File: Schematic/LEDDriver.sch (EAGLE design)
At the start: 33 parts, among them IC1 TL494CN, IC2 LM317, IC3 TL494CN, Q1 IRFZ44N, Q2 IRFZ44N, Q3 BC557, Q4 BC557

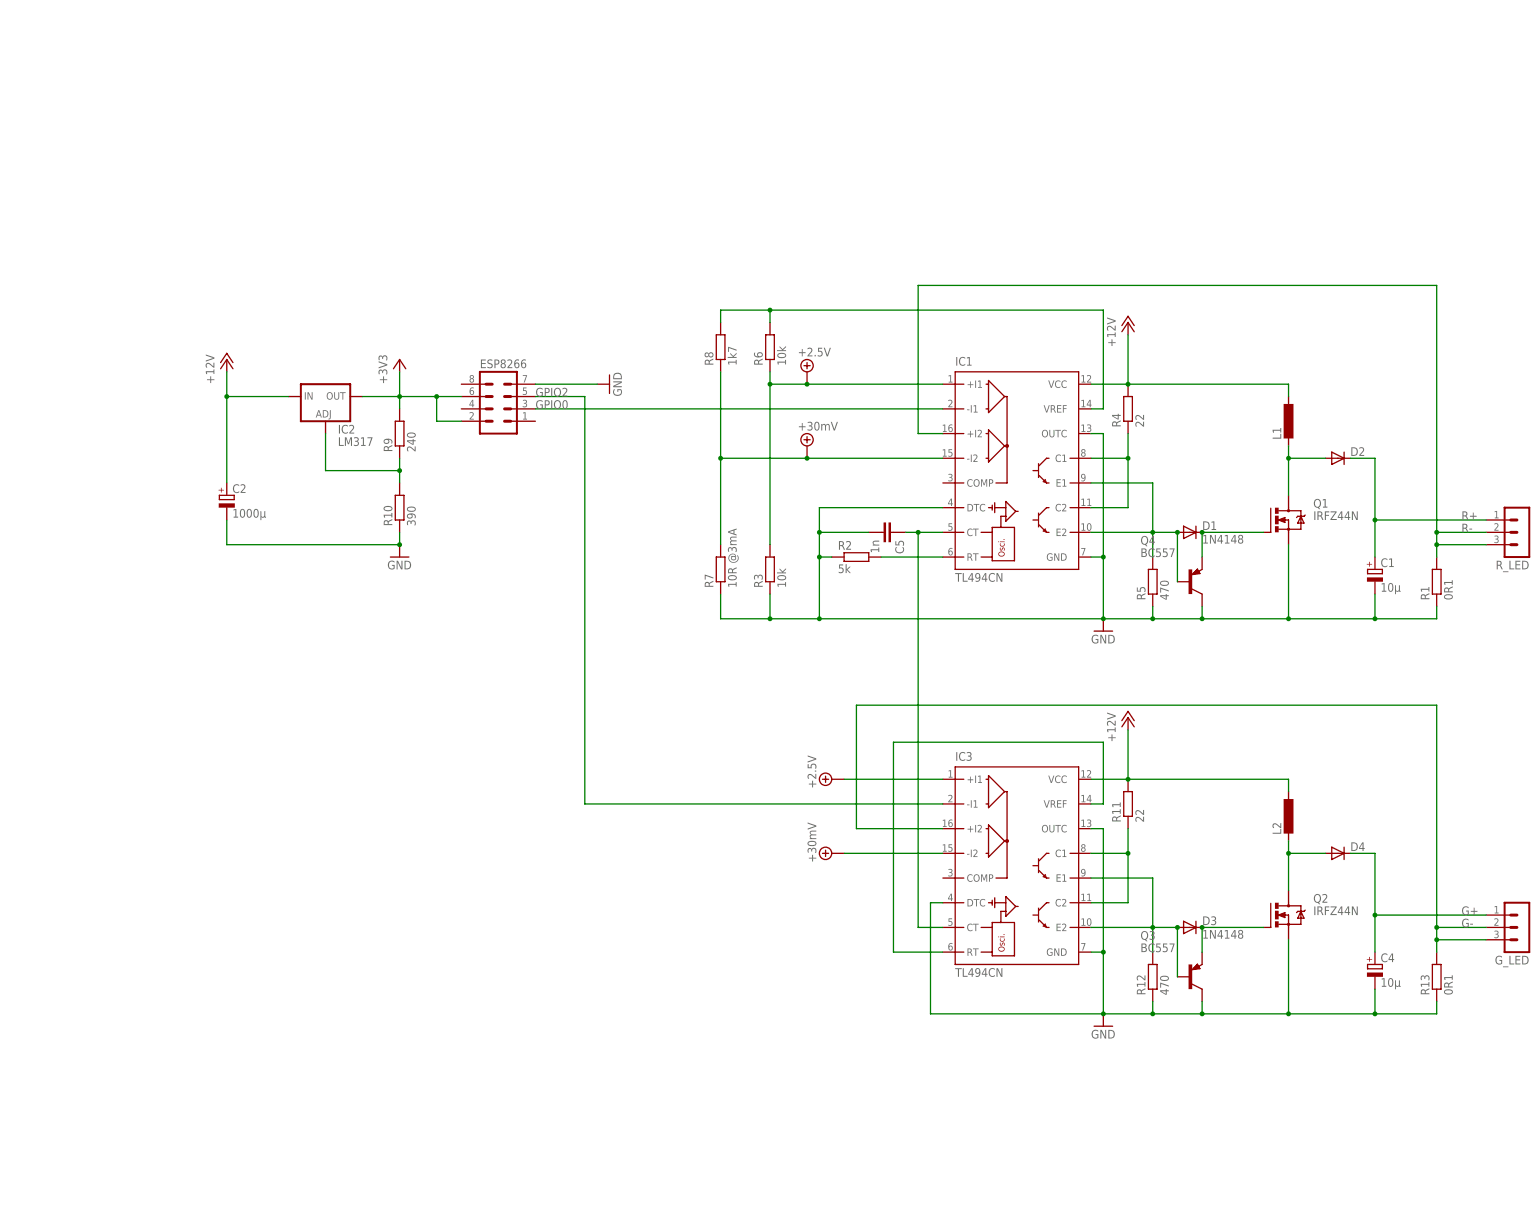
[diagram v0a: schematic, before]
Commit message: Use Xl6009 with op amp as  current source for leds
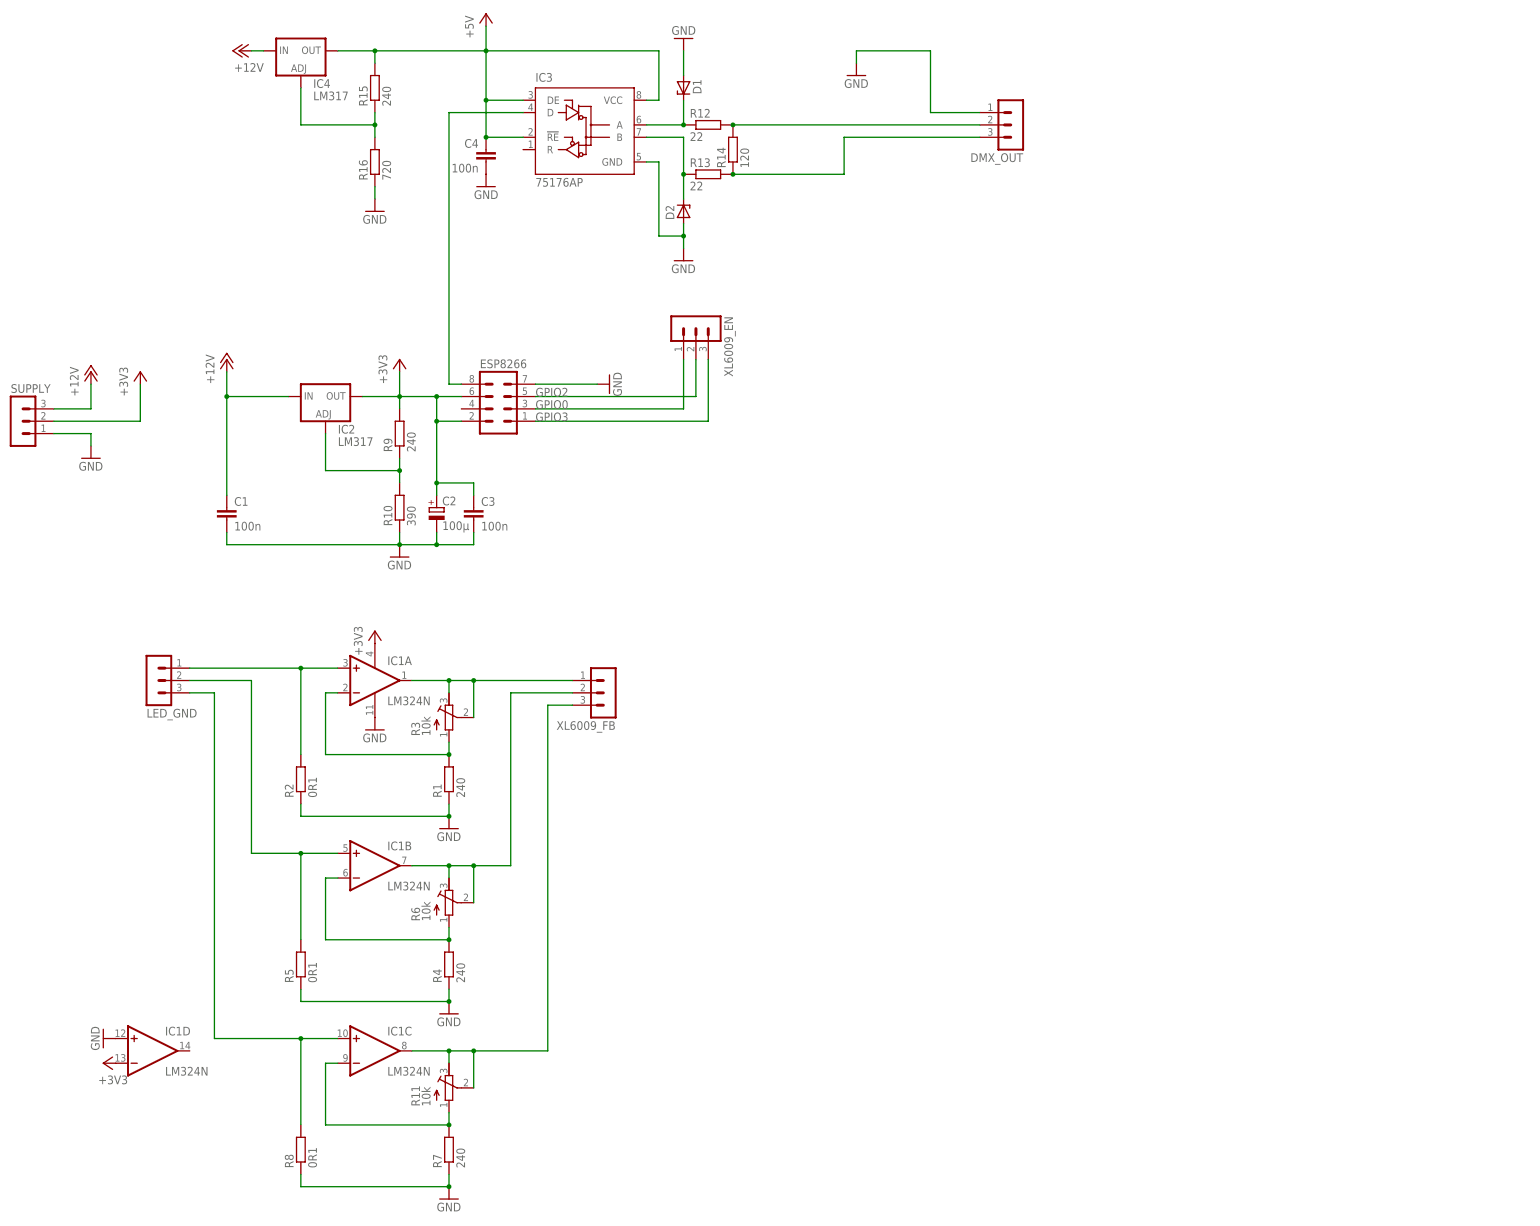
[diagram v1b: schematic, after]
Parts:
- removed C5: 1n, rcl:C-EU025-024X044
- removed D3: 1N4148, diode:DIODE-D-2.5
- removed D4: (no value), diode:DIODE-D-2.5
- removed G_LED, R_LED: (no value), con-lstb:MA03-1
- removed L1, L2: (no value), rcl:L-EU0204/5
- removed Q1, Q2: IRFZ44N, transistor-power:IRFZ48Z
- removed Q3, Q4: BC557, transistor-pnp:BC557
- added C3: 100n, rcl:C-EU075-032X103
- added DMX_OUT, LED_GND, SUPPLY, XL6009_EN, XL6009_FB: (no value), con-lstb:MA03-1
- added IC4: LM317, v-reg:LM317TS
- added R14: 120, rcl:R-EU_0204/2V
- added R15: 240, rcl:R-EU_0204/2V
- added R16: 720, rcl:R-EU_0207/10
- C1, C4: value 10µ -> 100n; device rcl:CPOL-EUE2.5-6 -> rcl:C-EU075-032X103
- C2: value 1000µ -> 100µ
- D1: value 1N4148 -> (none); device diode:DIODE-D-2.5 -> diode:ZENER-DIODEZD-2.5
- D2: device diode:DIODE-D-2.5 -> diode:ZENER-DIODEDO34-7
- IC1: value TL494CN -> LM324N; device linear:TL494CN -> linear:LM324N
- IC3: value TL494CN -> 75176AP; device linear:TL494CN -> 751xx:75176AP
- R1: value 0R1 -> 240; device rcl:R-EU_0204/7 -> rcl:R-EU_0204/2V
- R10: device rcl:R-EU_0207/10 -> rcl:R-EU_0207/12
- R11: value 22 -> 10k; device rcl:R-EU_0204/2V -> rcl:R-TRIMM64W
- R12: value 470 -> 22
- R13: value 0R1 -> 22; device rcl:R-EU_0204/7 -> rcl:R-EU_0204/2V
- R2: value 5k -> 0R1
- R3: device rcl:R-EU_0204/2V -> rcl:R-TRIMM64W
- R4: value 22 -> 240
- R5: value 470 -> 0R1
- R6: device rcl:R-EU_0204/7 -> rcl:R-TRIMM64W
- R7: value 10R @3mA -> 240
- R8: value 1k7 -> 0R1
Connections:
- removed net +30MV: IC1.-I2, IC3.-I2, R7.2, R8.1
- removed net +4.1V: IC1.+I1, IC3.+I1, R3.2, R6.1
- removed net G+: C4.+, D4.C, G_LED.1
- removed net G-: G_LED.2, G_LED.3, IC3.+I2, R13.2
- removed net N$17: IC3.C1, IC3.C2, R11.1
- removed net N$18: D3.A, IC3.E1, IC3.E2, Q3.B, R12.2
- removed net N$19: D4.A, L2.2, Q2.D
- removed net R+: C1.+, D2.C, R_LED.1
- removed net R-: IC1.+I2, R1.2, R_LED.2, R_LED.3
- new net +5V: C4.1, IC3.!RE, IC3.DE, IC3.VCC, IC4.OUT, R15.2
- new net DMX2: DMX_OUT.2, R12.2, R14.2
- new net GPIO3: ESP8266.1, XL6009_EN.3
- new net N$10: IC1C.+IN, LED_GND.3, R8.2
- new net N$14: D1.C, IC3.A, R12.1
- new net N$15: D2.C, IC3.B, R13.1
- new net N$4: IC1A.OUT, R3.E, R3.S, XL6009_FB.1
- new net N$9: IC1B.-IN, R4.2, R6.A
- net +12V: now also C1.1, IC4.IN, SUPPLY.3; no longer C2.+, IC1.VCC, IC3.VCC, L1.1, L2.1, R11.2, R4.2
- net +3V3: now also C2.+, C3.1, IC1D.-IN, IC1P.V+, SUPPLY.2
- net GND: now also C1.2, C3.2, C4.2, D1.A, D2.A, DMX_OUT.1, IC1D.+IN, IC1P.V-, R16.1, R4.1, R8.1, SUPPLY.1; no longer C1.-, C4.-, C5.2, IC1.DTC, IC1.GND, IC1.OUTC, IC3.DTC, IC3.OUTC, Q1.S, Q2.S, Q3.C, Q4.C, R12.1, R13.1, R3.1
- net GPIO0: now also XL6009_EN.1; no longer IC1.-I1
- net GPIO2: now also XL6009_EN.2; no longer IC3.-I1
- net N$1: now also ESP8266.8, IC3.D; no longer D2.A, L1.2, Q1.D
- net N$11: now also IC1C.OUT, R11.E, R11.S, XL6009_FB.3; no longer IC1.C1, IC1.C2, R4.1
- net N$12: now also IC1C.-IN, R11.A, R7.2; no longer D1.A, IC1.E1, IC1.E2, Q4.B, R5.2
- net N$16: now also DMX_OUT.3, R13.2, R14.1; no longer D3.C, Q2.G, Q3.E
- net N$2: now also IC1A.-IN, R1.2, R3.A; no longer C5.1, IC1.CT, IC3.CT
- net N$3: now also IC1A.+IN, LED_GND.1, R2.2; no longer IC3.RT, IC3.VREF
- net N$6: now also IC1B.+IN, LED_GND.2, R5.2; no longer IC1.RT, R2.2
- net N$7: now also IC1B.OUT, R6.E, R6.S, XL6009_FB.2; no longer IC1.VREF, R6.2, R8.2
- net N$8: now also IC4.ADJ, R15.1, R16.2; no longer D1.C, Q1.G, Q4.E
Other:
- moved on the sheet: C2, R1, R12, R13, R2, R4, R5, R7, R8

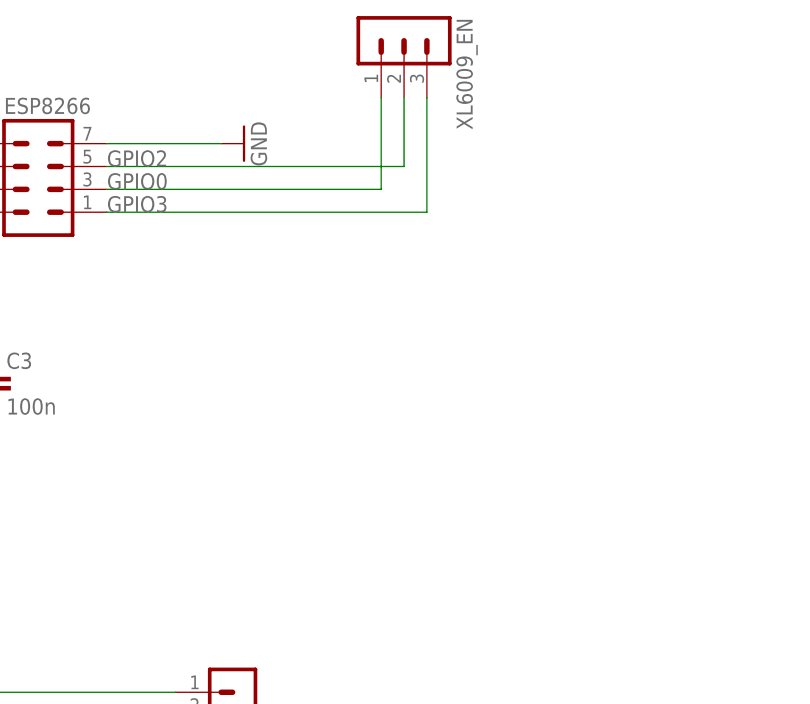
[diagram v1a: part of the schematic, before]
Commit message: Add pull downs to enable pins of LEDs to not flash up the LEDs on boot time
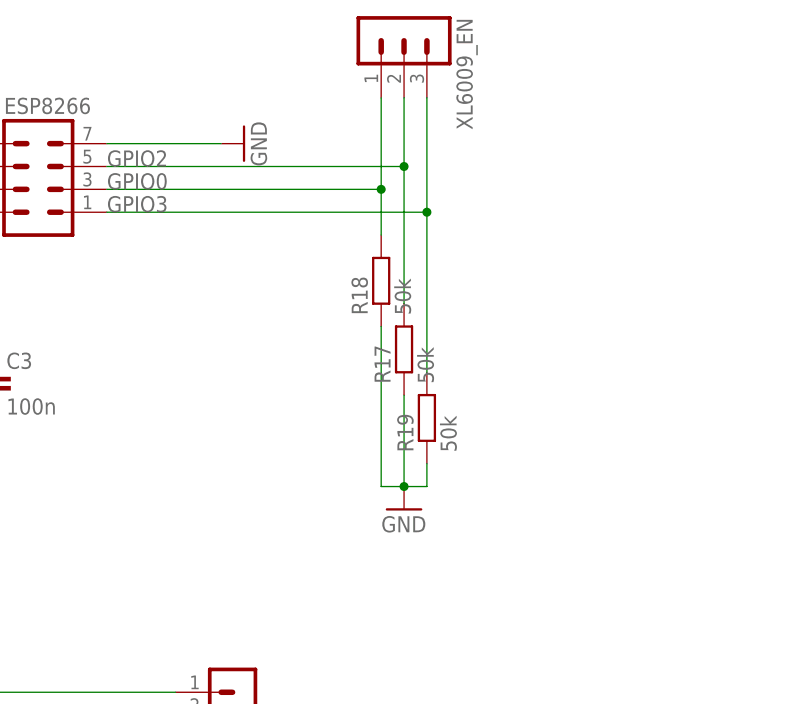
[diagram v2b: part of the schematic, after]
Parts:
- added R17, R18, R19: 50k, rcl:R-EU_0207/12
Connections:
- net GND: now also R17.1, R18.1, R19.1
- net GPIO0: now also R18.2
- net GPIO2: now also R17.2
- net GPIO3: now also R19.2
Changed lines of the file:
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@@
 <grid distance="0.1" unitdist="inch" unit="inch" style="lines" multiple="1" display="no" altdistance="0.01" altunitdist="inch" altunit="inch"/>
 <layers>
-<layer number="1" name="Top" color="4" fill="1" visible="yes" active="no"/>
-<layer number="16" name="Bottom" color="1" fill="1" visible="yes" active="no"/>
-<layer number="17" name="Pads" color="2" fill="1" visible="yes" active="no"/>
-<layer number="18" name="Vias" color="2" fill="1" visible="yes" active="no"/>
-<layer number="19" name="Unrouted" color="6" fill="1" visible="yes" active="no"/>
-<layer number="20" name="Dimension" color="15" fill="1" visible="yes" active="no"/>
-<layer number="21" name="tPlace" color="7" fill="1" visible="yes" active="no"/>
-<layer number="22" name="bPlace" color="7" fill="1" visible="yes" active="no"/>
-<layer number="23" name="tOrigins" color="15" fill="1" visible="yes" active="no"/>
-<layer number="24" name="bOrigins" color="15" fill="1" visible="yes" active="no"/>
-<layer number="25" name="tNames" color="7" fill="1" visible="yes" active="no"/>
-<layer number="26" name="bNames" color="7" fill="1" visible="yes" active="no"/>
-<layer number="27" name="tValues" color="7" fill="1" visible="yes" active="no"/>
-<layer number="28" name="bValues" color="7" fill="1" visible="yes" active="no"/>
+<layer number="1" name="Top" color="4" fill="1" visible="no" active="no"/>
+<layer number="16" name="Bottom" color="1" fill="1" visible="no" active="no"/>
+<layer number="17" name="Pads" color="2" fill="1" visible="no" active="no"/>
+<layer number="18" name="Vias" color="2" fill="1" visible="no" active="no"/>
+<layer number="19" name="Unrouted" color="6" fill="1" visible="no" active="no"/>
+<layer number="20" name="Dimension" color="15" fill="1" visible="no" active="no"/>
+<layer number="21" name="tPlace" color="7" fill="1" visible="no" active="no"/>
+<layer number="22" name="bPlace" color="7" fill="1" visible="no" active="no"/>
+<layer number="23" name="tOrigins" color="15" fill="1" visible="no" active="no"/>
+<layer number="24" name="bOrigins" color="15" fill="1" visible="no" active="no"/>
+<layer number="25" name="tNames" color="7" fill="1" visible="no" active="no"/>
+<layer number="26" name="bNames" color="7" fill="1" visible="no" active="no"/>
+<layer number="27" name="tValues" color="7" fill="1" visible="no" active="no"/>
+<layer number="28" name="bValues" color="7" fill="1" visible="no" active="no"/>
 <layer number="29" name="tStop" color="7" fill="3" visible="no" active="no"/>
 <layer number="30" name="bStop" color="7" fill="6" visible="no" active="no"/>
@@
 <layer number="35" name="tGlue" color="7" fill="4" visible="no" active="no"/>
 <layer number="36" name="bGlue" color="7" fill="5" visible="no" active="no"/>
-<layer number="37" name="tTest" color="7" fill="1" visible="yes" active="no"/>
-<layer number="38" name="bTest" color="7" fill="1" visible="yes" active="no"/>
+<layer number="37" name="tTest" color="7" fill="1" visible="no" active="no"/>
+<layer number="38" name="bTest" color="7" fill="1" visible="no" active="no"/>
 <layer number="39" name="tKeepout" color="4" fill="11" visible="no" active="no"/>
 <layer number="40" name="bKeepout" color="1" fill="11" visible="no" active="no"/>
@@
 <layer number="44" name="Drills" color="7" fill="1" visible="no" active="no"/>
 <layer number="45" name="Holes" color="7" fill="1" visible="no" active="no"/>
-<layer number="46" name="Milling" color="3" fill="1" visible="yes" active="no"/>
-<layer number="47" name="Measures" color="7" fill="1" visible="yes" active="no"/>
-<layer number="48" name="Document" color="7" fill="1" visible="yes" active="no"/>
-<layer number="49" name="Reference" color="7" fill="1" visible="yes" active="no"/>
-<layer number="50" name="dxf" color="7" fill="1" visible="yes" active="no"/>
-<layer number="51" name="tDocu" color="7" fill="1" visible="yes" active="no"/>
-<layer number="52" name="bDocu" color="7" fill="1" visible="yes" active="no"/>
-<layer number="53" name="tPadExt" color="7" fill="1" visible="yes" active="no"/>
-<layer number="54" name="bPadExt" color="1" fill="1" visible="yes" active="no"/>
+<layer number="46" name="Milling" color="3" fill="1" visible="no" active="no"/>
+<layer number="47" name="Measures" color="7" fill="1" visible="no" active="no"/>
+<layer number="48" name="Document" color="7" fill="1" visible="no" active="no"/>
+<layer number="49" name="Reference" color="7" fill="1" visible="no" active="no"/>
+<layer number="50" name="dxf" color="7" fill="1" visible="no" active="no"/>
+<layer number="51" name="tDocu" color="7" fill="1" visible="no" active="no"/>
+<layer number="52" name="bDocu" color="7" fill="1" visible="no" active="no"/>
+<layer number="53" name="tPadExt" color="7" fill="1" visible="no" active="no"/>
+<layer number="54" name="bPadExt" color="1" fill="1" visible="no" active="no"/>
 <layer number="91" name="Nets" color="2" fill="1" visible="yes" active="yes"/>
 <layer number="92" name="Busses" color="1" fill="1" visible="yes" active="yes"/>
@@
 <part name="R16" library="rcl" deviceset="R-EU_" device="0207/10" value="720"/>
 <part name="GND13" library="supply1" deviceset="GND" device=""/>
+<part name="R18" library="rcl" deviceset="R-EU_" device="0207/12" value="50k"/>
+<part name="R17" library="rcl" deviceset="R-EU_" device="0207/12" value="50k"/>
+<part name="R19" library="rcl" deviceset="R-EU_" device="0207/12" value="50k"/>
+<part name="GND14" library="supply1" deviceset="GND" device=""/>
 </parts>
 <sheets>
@@
 <instance part="R16" gate="G$1" x="-88.9" y="111.76" rot="R90"/>
 <instance part="GND13" gate="1" x="-88.9" y="101.6"/>
+<instance part="R18" gate="G$1" x="-25.4" y="50.8" rot="R90"/>
+<instance part="R17" gate="G$1" x="-22.86" y="43.18" rot="R90"/>
+<instance part="R19" gate="G$1" x="-20.32" y="35.56" rot="R90"/>
+<instance part="GND14" gate="1" x="-22.86" y="25.4"/>
 </instances>
 <busses>
@@
 <wire x1="-88.9" y1="106.68" x2="-88.9" y2="104.14" width="0.1524" layer="91"/>
 <pinref part="GND13" gate="1" pin="GND"/>
+</segment>
+<segment>
+<pinref part="R19" gate="G$1" pin="1"/>
+<wire x1="-20.32" y1="30.48" x2="-20.32" y2="27.94" width="0.1524" layer="91"/>
+<pinref part="R17" gate="G$1" pin="1"/>
+<wire x1="-20.32" y1="27.94" x2="-22.86" y2="27.94" width="0.1524" layer="91"/>
+<wire x1="-22.86" y1="27.94" x2="-22.86" y2="38.1" width="0.1524" layer="91"/>
+<pinref part="R18" gate="G$1" pin="1"/>
+<wire x1="-22.86" y1="27.94" x2="-25.4" y2="27.94" width="0.1524" layer="91"/>
+<wire x1="-25.4" y1="27.94" x2="-25.4" y2="45.72" width="0.1524" layer="91"/>
+<junction x="-22.86" y="27.94"/>
+<pinref part="GND14" gate="1" pin="GND"/>
 </segment>
 </net>
@@
 <wire x1="-55.88" y1="63.5" x2="-22.86" y2="63.5" width="0.1524" layer="91"/>
 <wire x1="-22.86" y1="63.5" x2="-22.86" y2="71.12" width="0.1524" layer="91"/>
+<pinref part="R17" gate="G$1" pin="2"/>
+<wire x1="-22.86" y1="48.26" x2="-22.86" y2="63.5" width="0.1524" layer="91"/>
+<junction x="-22.86" y="63.5"/>
 </segment>
 </net>
@@
 <wire x1="-25.4" y1="60.96" x2="-25.4" y2="71.12" width="0.1524" layer="91"/>
 <label x="-55.88" y="60.96" size="1.778" layer="95"/>
+<pinref part="R18" gate="G$1" pin="2"/>
+<wire x1="-25.4" y1="55.88" x2="-25.4" y2="60.96" width="0.1524" layer="91"/>
+<junction x="-25.4" y="60.96"/>
 </segment>
 </net>
@@
 <wire x1="-20.32" y1="58.42" x2="-20.32" y2="71.12" width="0.1524" layer="91"/>
 <label x="-55.88" y="58.42" size="1.778" layer="95"/>
-</segment>
-</net>
+<pinref part="R19" gate="G$1" pin="2"/>
+<wire x1="-20.32" y1="40.64" x2="-20.32" y2="58.42" width="0.1524" layer="91"/>
+<junction x="-20.32" y="58.42"/>
+</segment>
+</net>
